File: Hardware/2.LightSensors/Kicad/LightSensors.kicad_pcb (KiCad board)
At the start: 2 copper layers, 45 x 25 mm, 20 parts, among them J1 Conn_01x10_Pin, U1 AS7331, U2 OPT3004

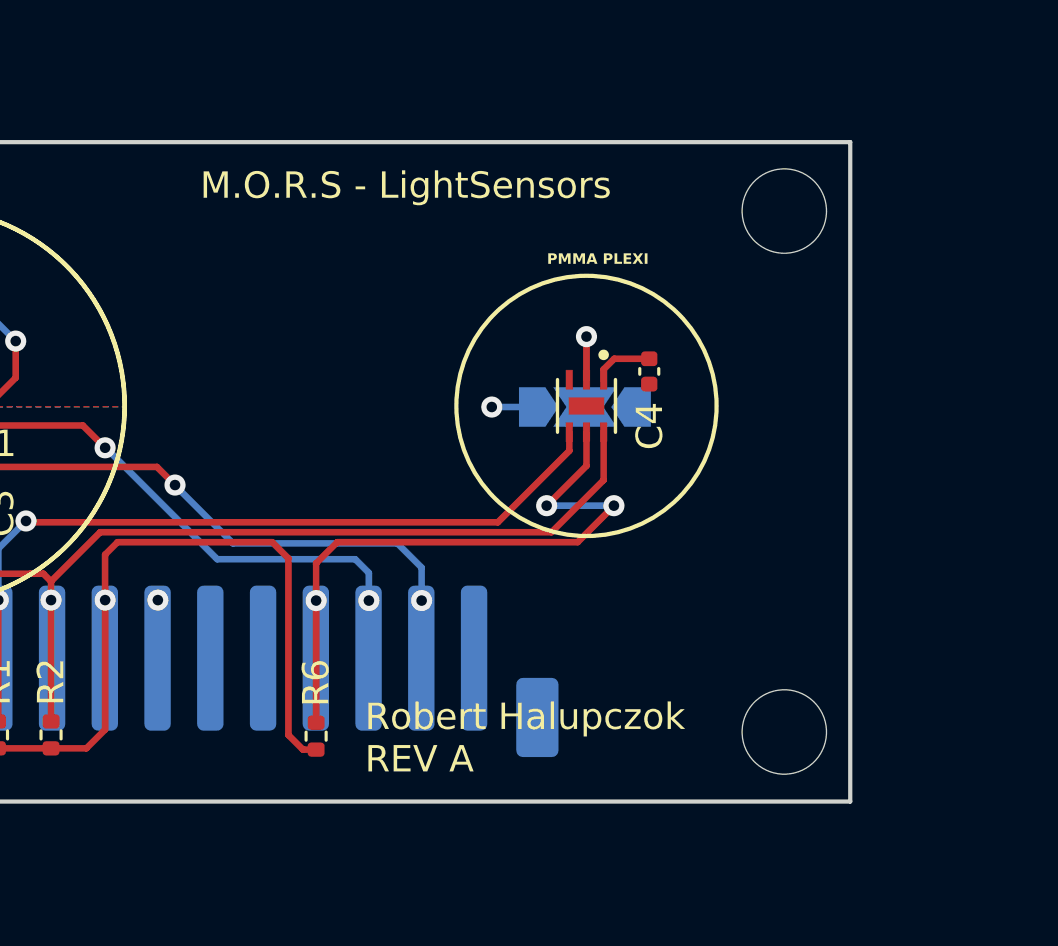
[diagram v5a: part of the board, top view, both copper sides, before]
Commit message: Add logo into pcb and update silkscreen
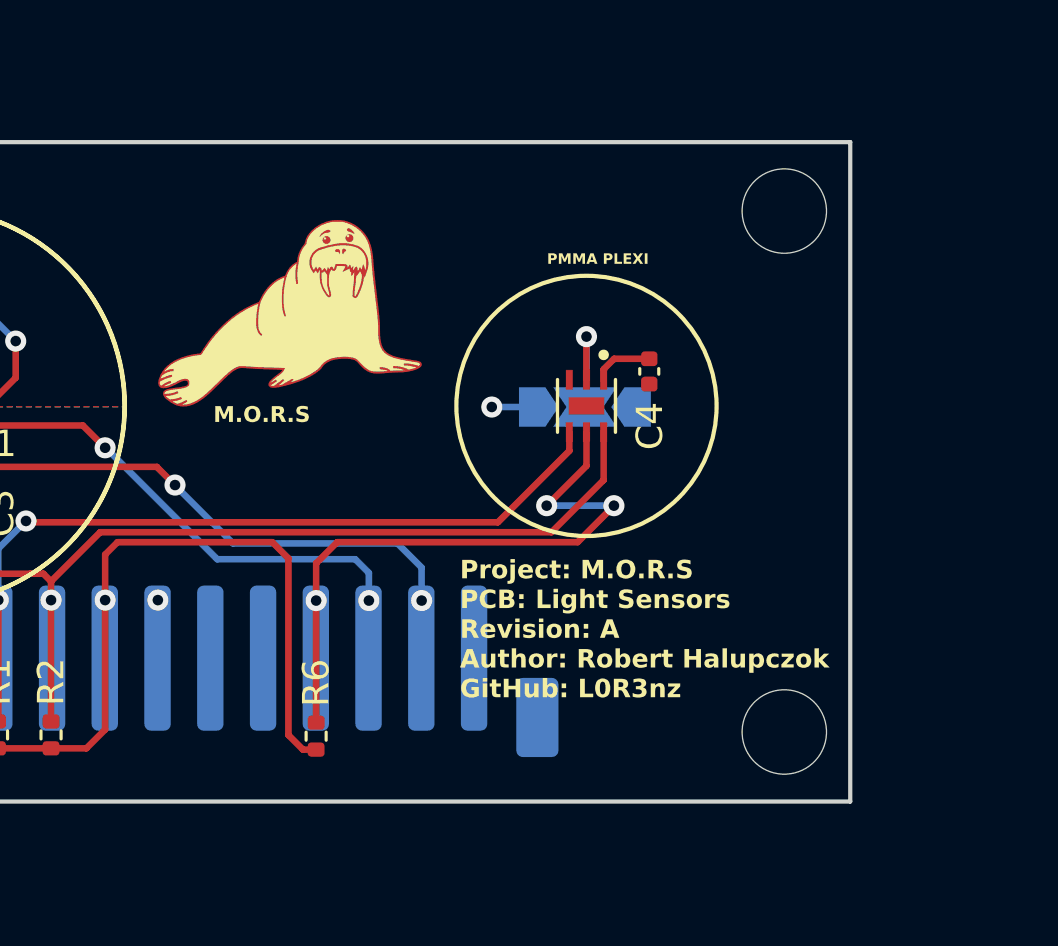
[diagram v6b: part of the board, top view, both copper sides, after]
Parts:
- added G***: LOGO, Mors_logo:MORS_logo_10mm, F.Cu at (103.1, 111.8)
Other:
- board text added: "M.O.R.S"
- board text added: "Project: M.O.R.S PCB: Light Sensors Revision: A Author: Robert Halupczok GitHub: L0R3nz"
- board text removed: "M.O.R.S - LightSensors"
- board text removed: "Robert Halupczok REV A"
